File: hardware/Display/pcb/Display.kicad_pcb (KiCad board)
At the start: 2 copper layers, 48 x 17 mm, 6 parts, among them J1 Conn_01x05, U3 74HC595, U4 HD44780

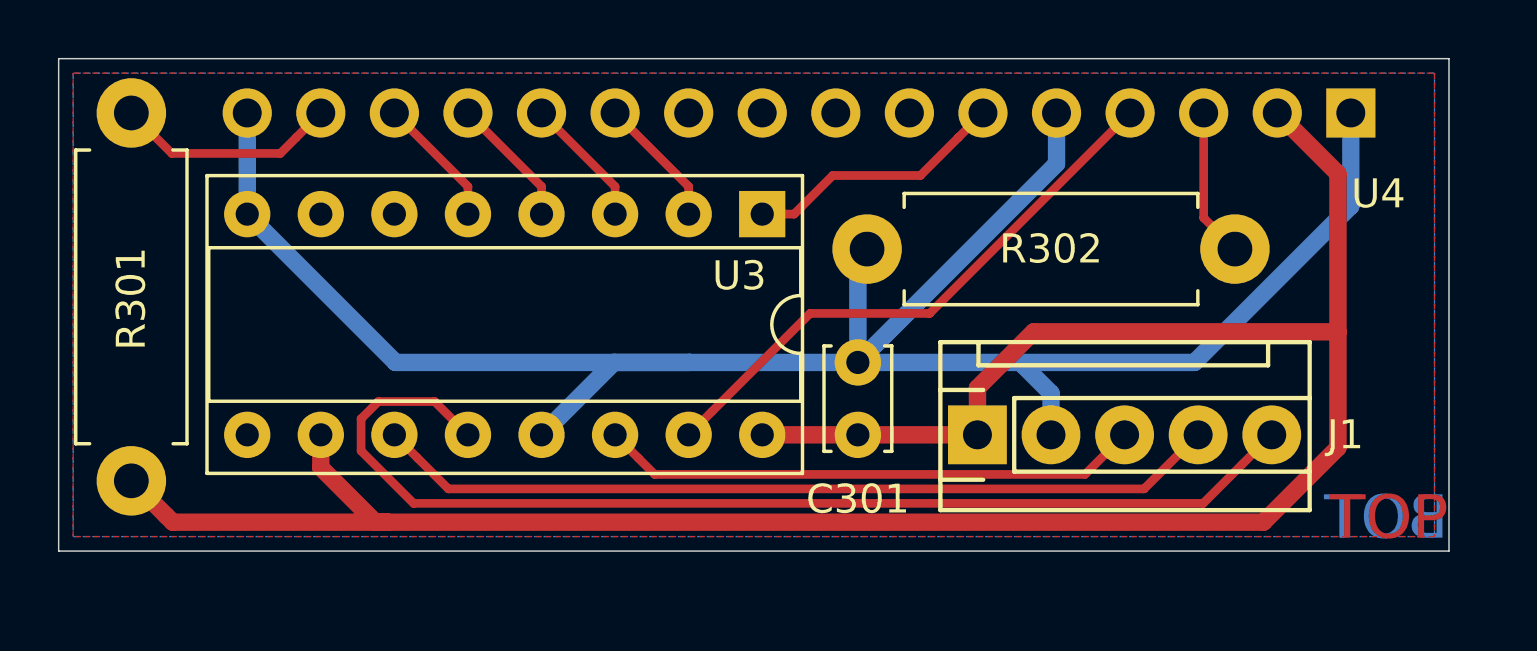
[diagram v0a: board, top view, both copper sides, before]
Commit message: feat: General PCB improvements
fix Display, add BOM

Issue #14
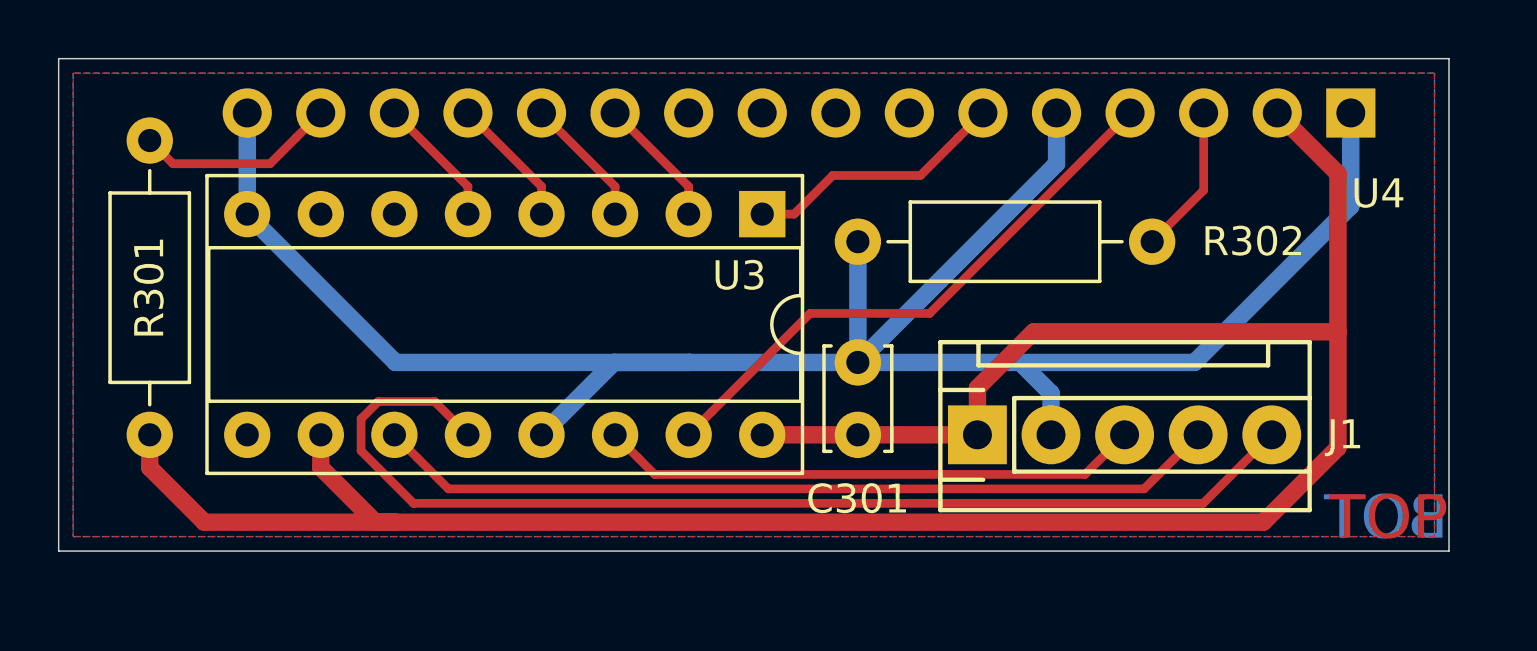
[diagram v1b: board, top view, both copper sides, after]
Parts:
- R301, R302: footprint Resistor_THT:R_Axial_DIN0411_L9.9mm_D3.6mm_P12.70mm_Horizontal -> Resistor_THT:R_Axial_DIN0207_L6.3mm_D2.5mm_P10.16mm_Horizontal
- moved R302 2.87 mm to (51.8, 20.3)
- moved R301 1.71 mm to (17.1, 27.0)
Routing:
- net +5V: track 82.3 -> 83.2 mm
- net Net-(R301-Pad2): track 7.70 -> 6.96 mm

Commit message: feat: General PCB improvements
redo Display

Issue #14
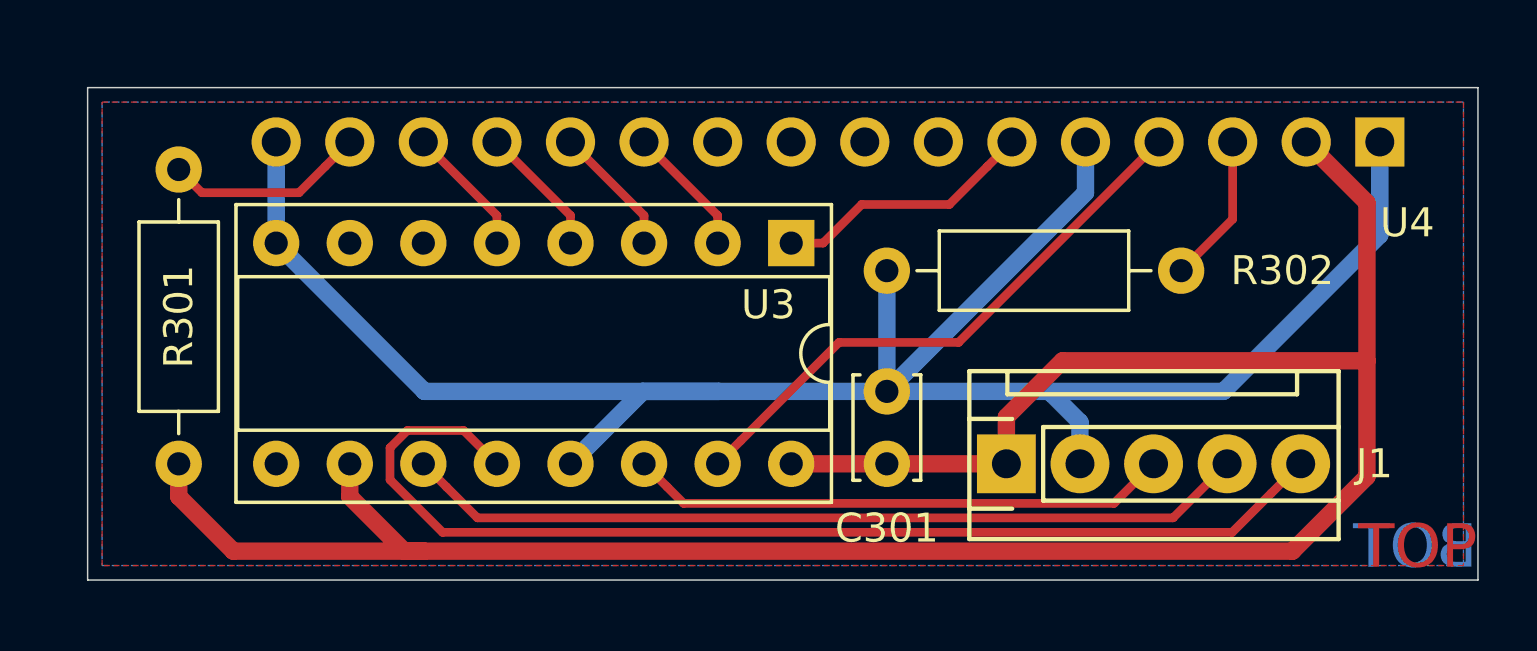
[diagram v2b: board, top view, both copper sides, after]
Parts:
- moved C301 1.41 mm to (42.6, 28.0)
- moved J1 1.41 mm to (46.7, 28.0)
- moved R301 1.41 mm to (18.1, 28.0)
- moved R302 1.41 mm to (52.8, 21.3)
- moved U3 1.41 mm to (39.3, 20.4)
- moved U4 1.41 mm to (59.6, 16.9)
